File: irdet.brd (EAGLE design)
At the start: 50 x 45 mm, 66 parts, among them IC1 MEGA8-AI, IC2 78L05F, J1 PSH02-04WG, J2 PSH02-04WG, J3 PSH02-04WG, J4 PSH02-04WG, J5 22-05-7098-09, T1 S9013, T2 S9012, T3 S9013, T4 S9012, T5 S9013, T6 S9012, T7 S9013, T8 S9012, X1 ARK500/2, X2 ARK500/2

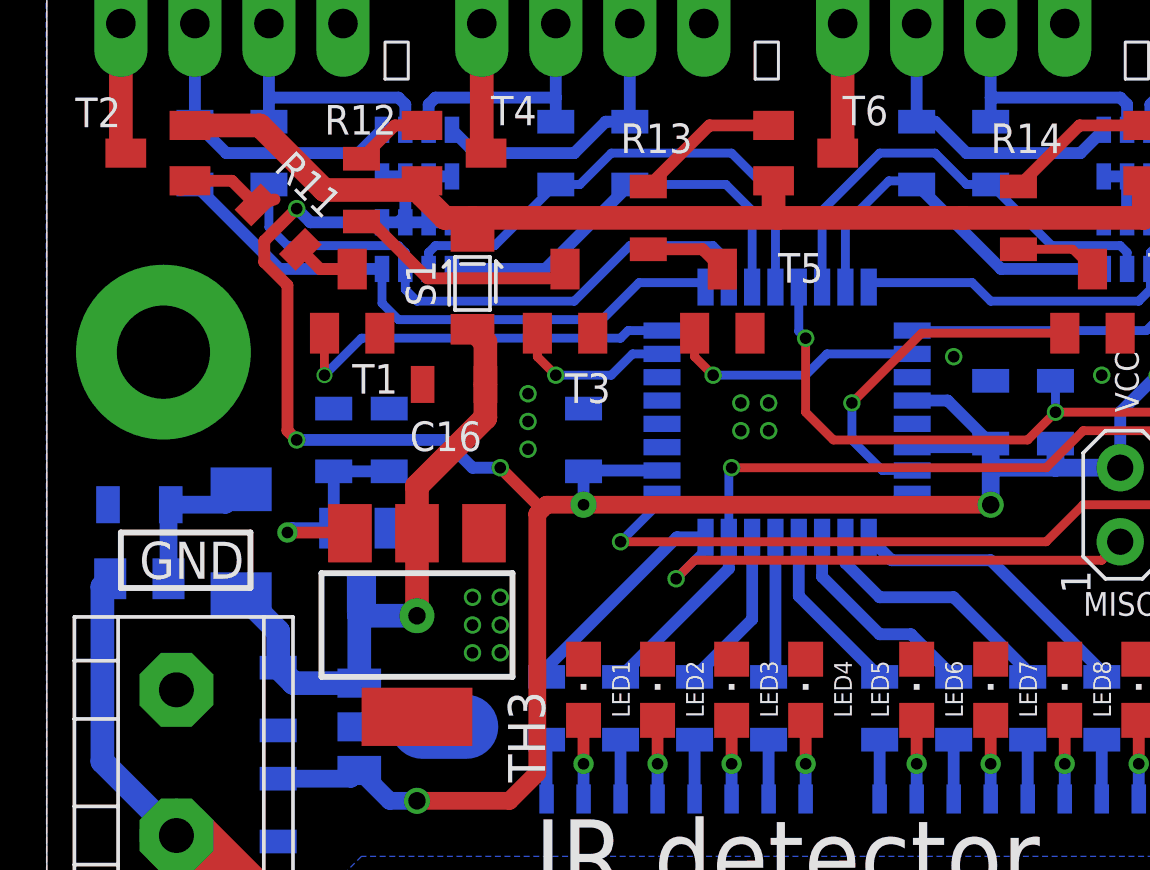
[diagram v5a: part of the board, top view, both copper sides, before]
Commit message: Brd: fix DRC errors & warnings.
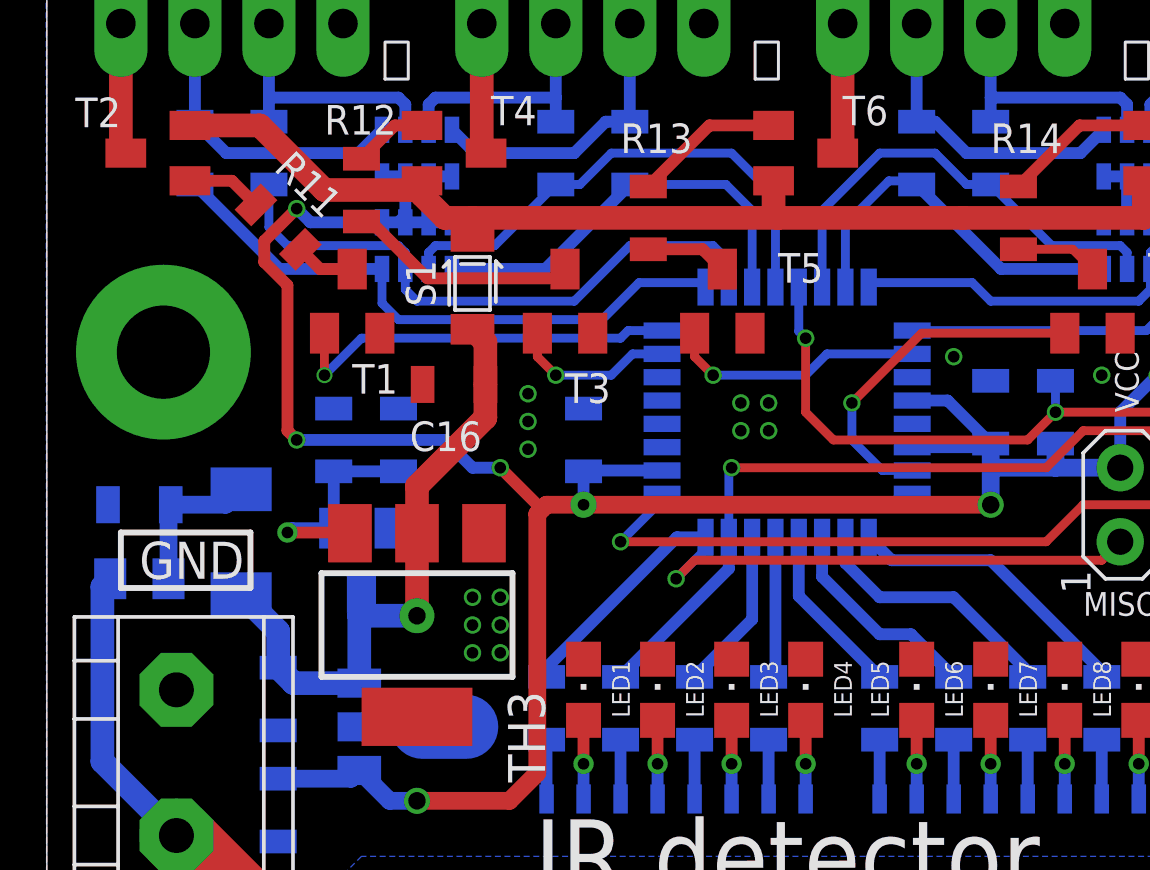
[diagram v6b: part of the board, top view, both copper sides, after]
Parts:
- moved R2 0.32 mm to (12.1, 27.0)
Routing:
- net N$13: track 3.72 -> 2.61 mm
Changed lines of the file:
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@@
 <attribute name="VALUE" x="30.7975" y="35.2425" size="1.27" layer="27" rot="R270"/>
 </element>
-<element name="R2" library="rcl" package="R0805" value="2k2" x="11.7475" y="26.9875" smashed="yes" rot="MR270">
-<attribute name="NAME" x="13.97" y="27.94" size="1.016" layer="26" rot="MR270"/>
-<attribute name="VALUE" x="14.2875" y="27.6225" size="1.27" layer="28" rot="MR270"/>
+<element name="R2" library="rcl" package="R0805" value="2k2" x="12.065" y="26.9875" smashed="yes" rot="MR270">
+<attribute name="NAME" x="14.2875" y="27.94" size="1.016" layer="26" rot="MR270"/>
+<attribute name="VALUE" x="14.605" y="27.6225" size="1.27" layer="28" rot="MR270"/>
 </element>
 <element name="R3" library="rcl" package="R0805" value="1k" x="28.575" y="17.78" smashed="yes" rot="MR270">
@@
 <wire x1="9.845" y1="23.96" x2="9.845" y2="25.908" width="0.4064" layer="16"/>
 <wire x1="9.845" y1="25.908" x2="9.8425" y2="25.9105" width="0.4064" layer="16"/>
-<wire x1="9.8425" y1="25.9105" x2="11.7475" y2="25.9105" width="0.4064" layer="16"/>
+<wire x1="9.8425" y1="25.9105" x2="12.065" y2="25.9105" width="0.4064" layer="16"/>
 <wire x1="9.845" y1="23.96" x2="8.4025" y2="23.96" width="0.4064" layer="16"/>
 <wire x1="8.4025" y1="23.96" x2="8.255" y2="23.8125" width="0.4064" layer="16"/>
@@
 <wire x1="12.7" y1="23.7875" x2="12.7" y2="20.955" width="0.8128" layer="1"/>
 <via x="12.7" y="20.955" extent="1-16" drill="0.6" diameter="1.2"/>
-<wire x1="10.719" y1="18.644" x2="10.719" y2="18.974" width="0.8128" layer="16"/>
 <wire x1="14.605" y1="30.785" x2="15.047" y2="30.343" width="0.8128" layer="1"/>
 <wire x1="15.047" y1="30.343" x2="15.047" y2="28.8925" width="0.8128" layer="1"/>
@@
 <contactref element="T2" pad="B"/>
 <contactref element="R11" pad="1"/>
-<wire x1="4.91" y1="35.88" x2="4.59561875" y2="35.56" width="0.4064" layer="1"/>
-<wire x1="7.17594375" y1="35.051553125" x2="7.813" y2="35.2425" width="0.4064" layer="1"/>
 <wire x1="4.91" y1="35.88" x2="6.347496875" y2="35.88" width="0.4064" layer="1"/>
 <wire x1="6.347496875" y1="35.88" x2="7.17594375" y2="35.051553125" width="0.4064" layer="1"/>
@@
 <wire x1="12.5525" y1="35.5625" x2="12.87" y2="35.88" width="0.8128" layer="1"/>
 <wire x1="7.305" y1="37.78" x2="9.5225" y2="35.5625" width="0.8128" layer="1"/>
-<wire x1="31.43" y1="34.605" x2="31.4325" y2="34.6075" width="0.8128" layer="1"/>
 <wire x1="14.605" y1="33.97" x2="14.605" y2="34.6075" width="0.8128" layer="1"/>
 </signal>
